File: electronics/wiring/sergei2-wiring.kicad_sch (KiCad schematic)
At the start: 27 parts, among them J1 6i25 port 1, J2 6i25 port 2, M1 UGRMEM, M2 UGRMEM, M3 MY1016, M4 Spindle, SW1 ESTOP, SW2 Mode switch, SW3 Run, SW4 Door closed, SW5 Pause, U1 Power_control_PCB

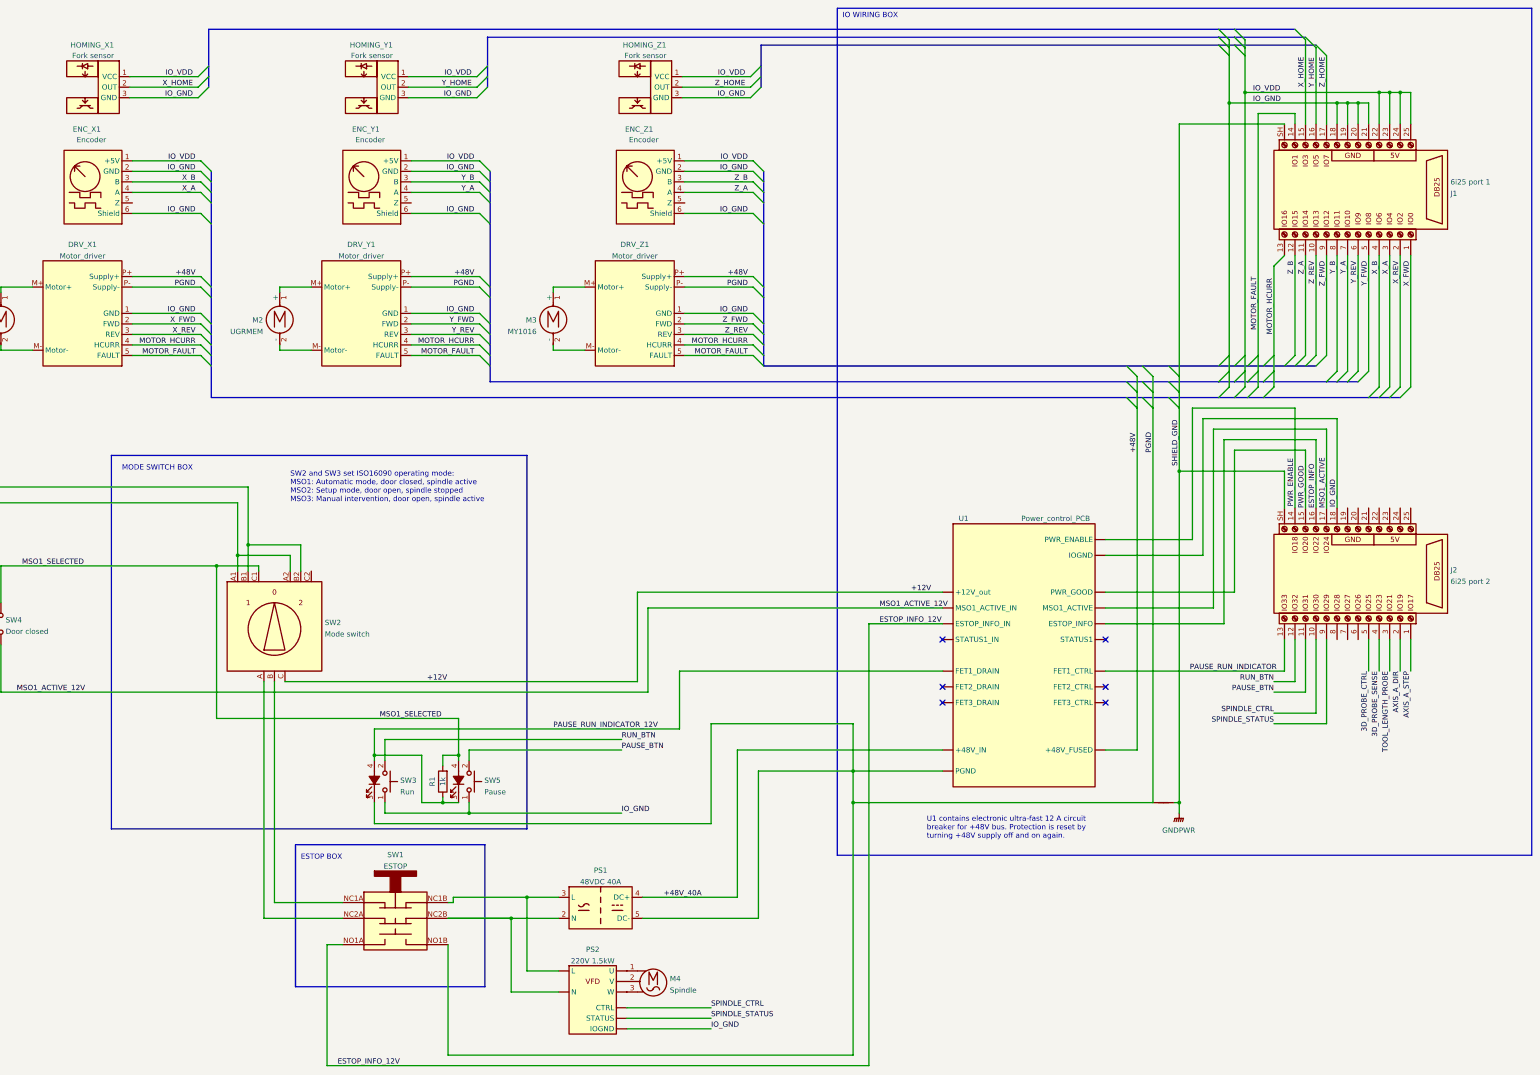
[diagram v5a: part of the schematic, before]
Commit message: Add PWM output for spindle control
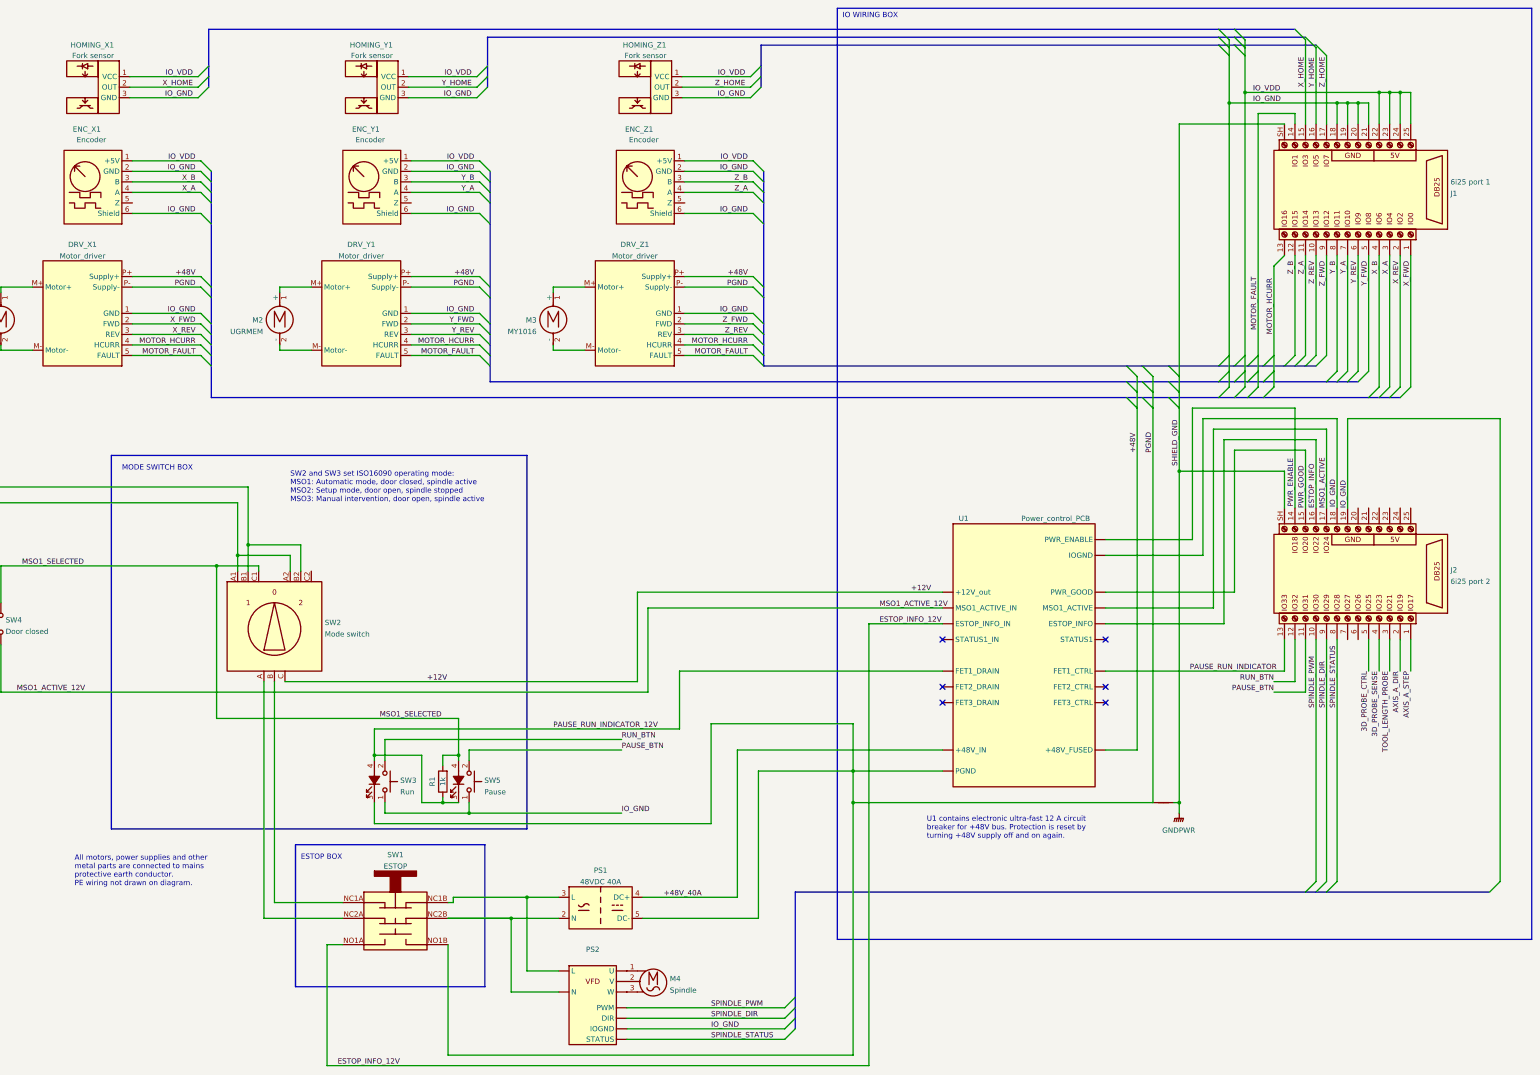
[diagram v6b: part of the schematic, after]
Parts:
- PS2: value 220V 1.5kW -> (none)
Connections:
- net IO_GND: now also J2.19
- net SPINDLE_STATUS: now also J2.8; no longer J2.9
- net SPINDLE_CTRL renamed SPINDLE_PWM
- new net SPINDLE_DIR: J2.9, PS2. (STATUS)
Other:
- note added: "All motors, power supplies and other metal parts are connected to mains protective earth conductor. PE wiring not drawn on diagram."

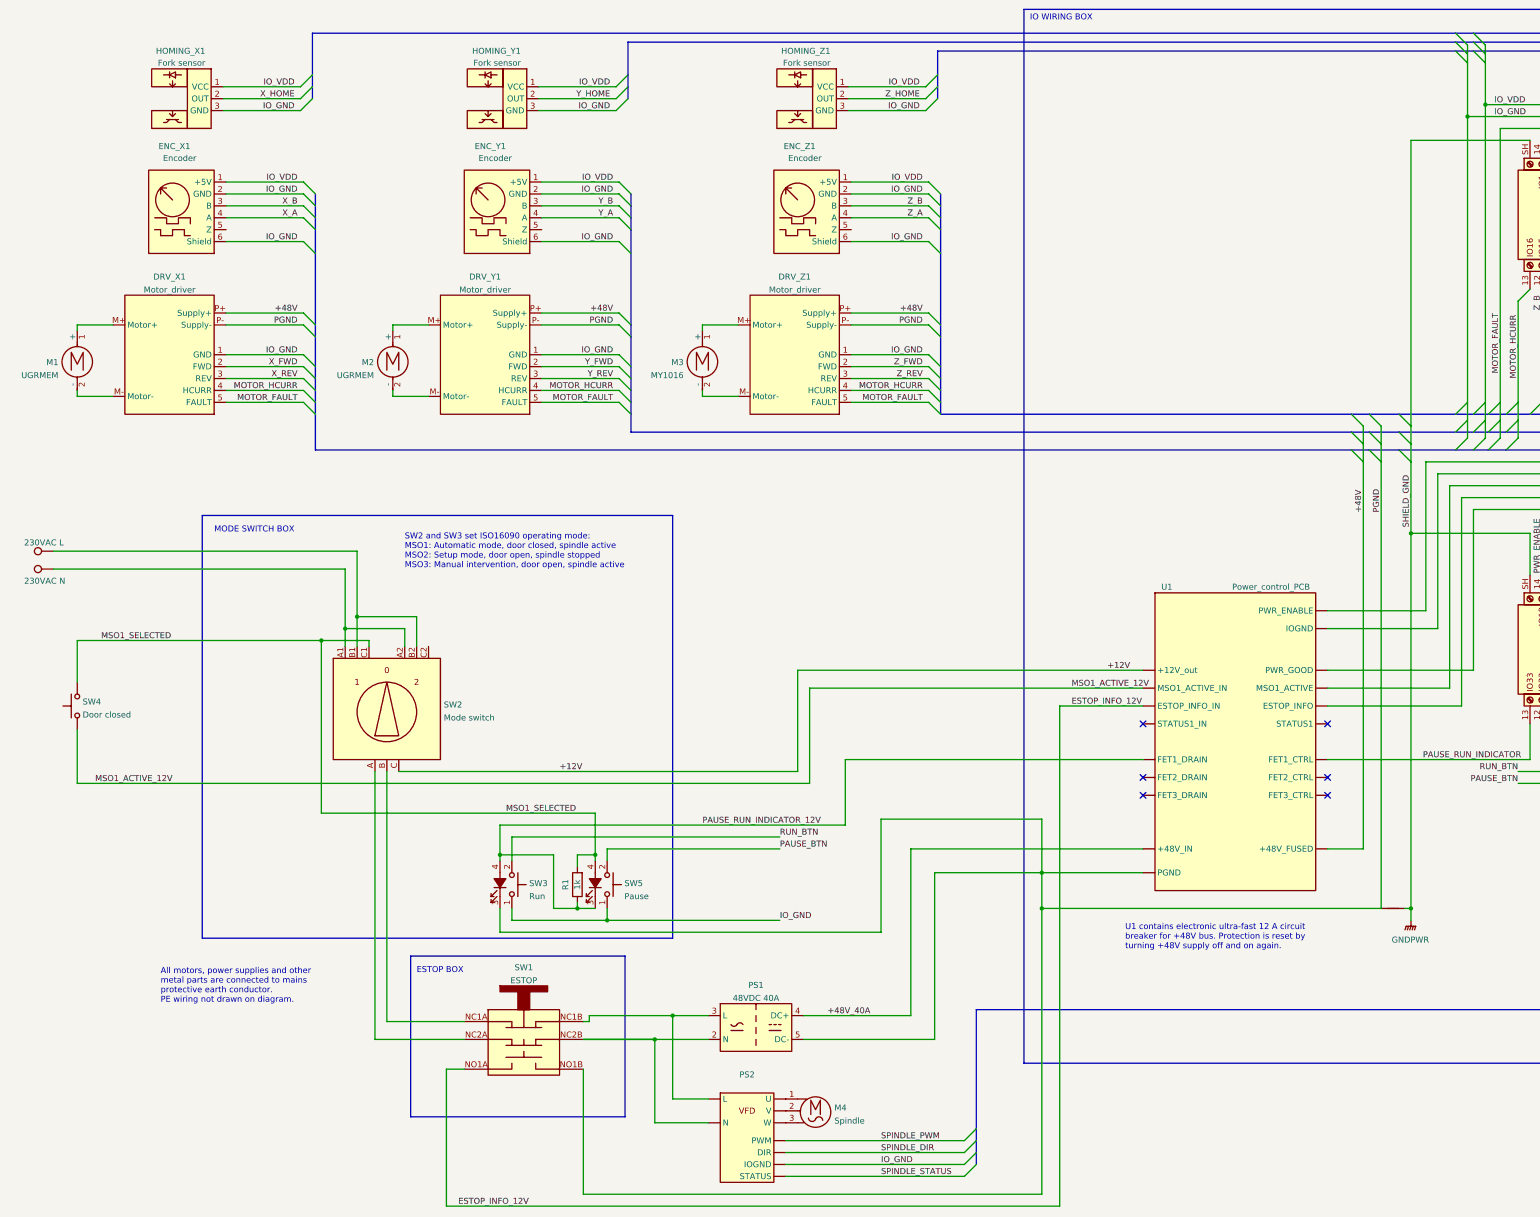
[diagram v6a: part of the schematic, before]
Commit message: Use FSESC 4.20 for driving Z axis, add brake shunt
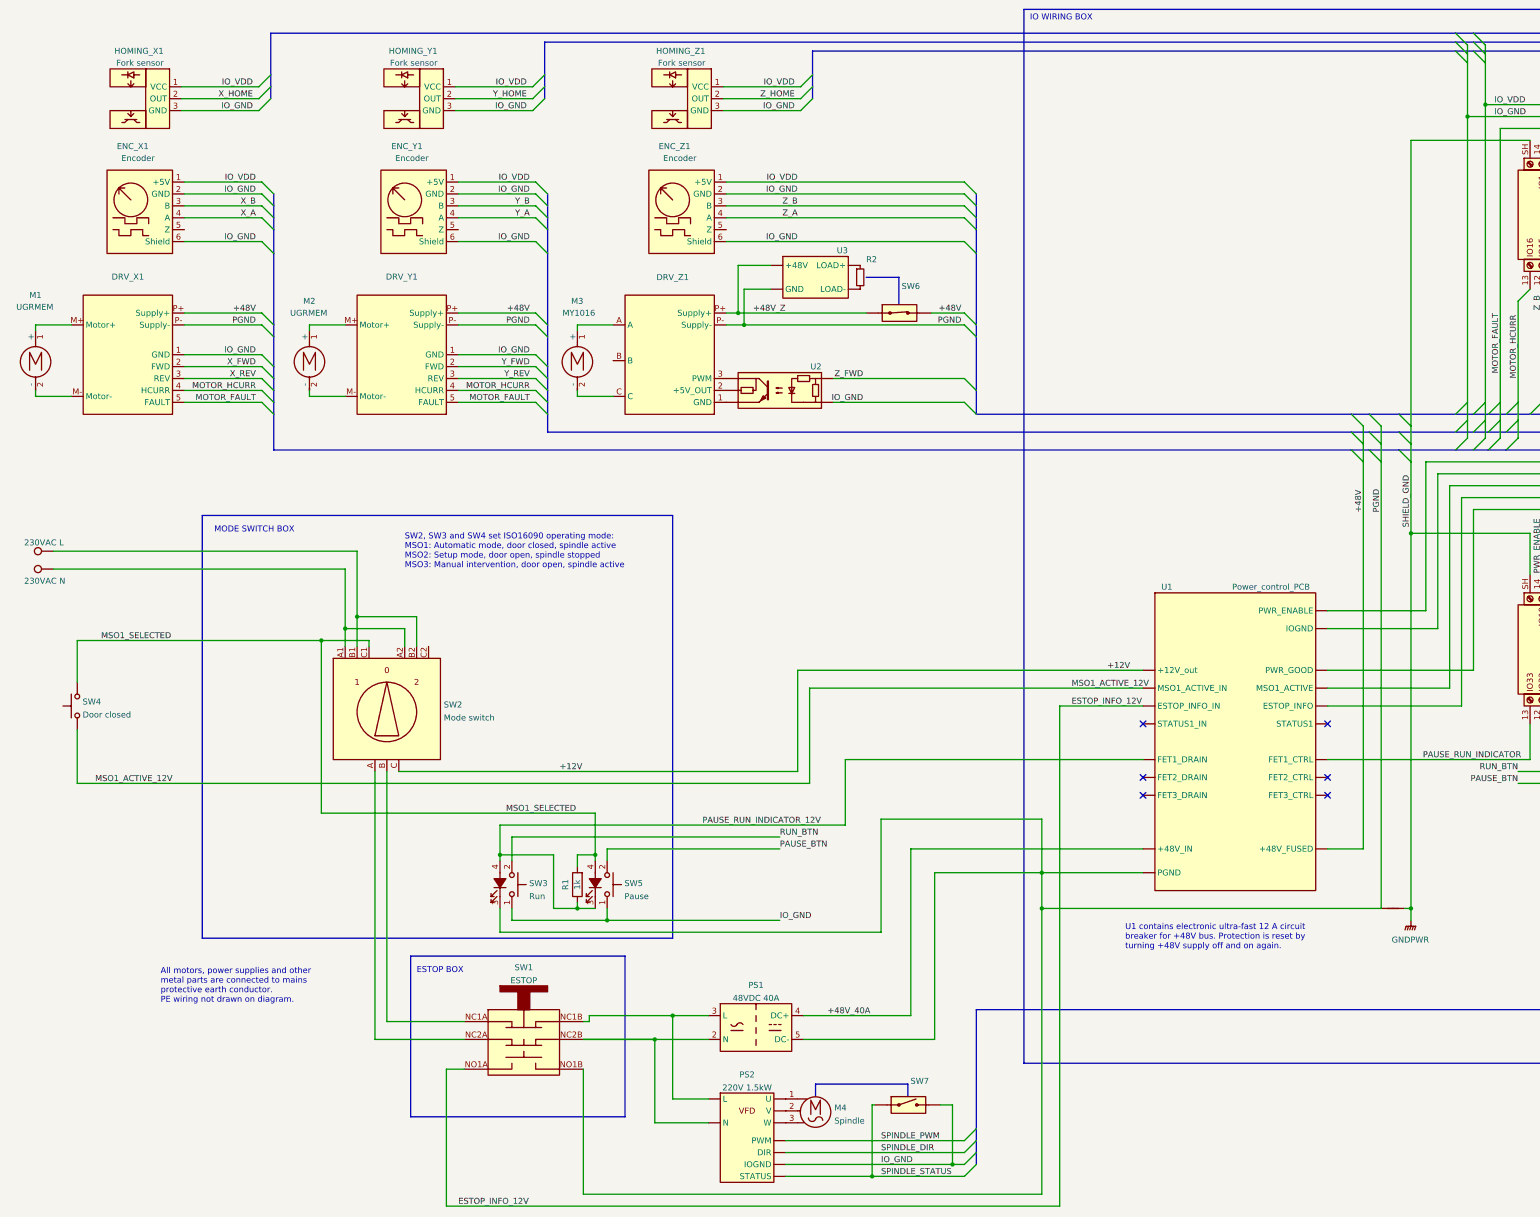
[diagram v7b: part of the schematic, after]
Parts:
- removed DRV_Z1: Motor_driver, symbol sergei2_wiring:Motor_driver
- added DRV_Z1: (no value), symbol sergei2_wiring:Motor_driver_FSESC
- added R2: (no value), symbol Device:R_Small
- added SW6: (no value), symbol sergei2_wiring:THERMAL_SW_NC
- added SW7: (no value), symbol sergei2_wiring:THERMAL_SW_NO
- added U2: (no value), symbol sergei2_wiring:OptoIsolator
- added U3: (no value), symbol sergei2_wiring:BrakeShunt
- DRV_X1, DRV_Y1: value Motor_driver -> (none)
- PS2: value (none) -> 220V 1.5kW
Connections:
- net +48V: now also SW6.
- net IO_GND: now also SW7., U2.2
- net PGND: now also DRV_Z1.P- (Supply-), U3. (LOAD-)
- net SPINDLE_STATUS: now also SW7.
- net Z_FWD: now also U2.1
- net at M3.1 (+): now also DRV_Z1.A
- net at M3.2 (-): now also DRV_Z1.C
- new net: DRV_Z1.1 (GND), U2.3
- new net: DRV_Z1.2 (+5V_OUT), U2.4
- new net: DRV_Z1.3 (PWM), U2.4
- new net: R2.1, U3. (LOAD-)
- new net: R2.2, U3. (LOAD-)
- new net +48V_Z: DRV_Z1.P+ (Supply+), SW6., U3. (LOAD-)
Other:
- note added: "SW2, SW3 and SW4 set ISO16090 operating mode: MSO1: Automatic mode, door closed, spindle active MSO2: Setup mode, door open, spindle stopped MSO3: Manual intervention, door open, spindle active"
- note removed: "SW2 and SW3 set ISO16090 operating mode: MSO1: Automatic mode, door closed, spindle active MSO2: Setup mode, door open, spindle stopped MSO3: Manual intervention, door open, spindle active"
- moved on the sheet: DRV_X1, DRV_Y1, ENC_X1, ENC_Y1, ENC_Z1, HOMING_X1, HOMING_Y1, HOMING_Z1, M1, M2, M3

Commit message: Misc configuration
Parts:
- removed SW6: (no value), symbol sergei2_wiring:THERMAL_SW_NC
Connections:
- net +48V: now also DRV_Z1.P+ (Supply+), U3. (LOAD-)
- removed net +48V_Z: DRV_Z1.P+ (Supply+), U3. (LOAD-)
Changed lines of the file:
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@@
   (junction (at 351.79 40.64) (diameter 0) (color 0 0 0 0)
   )
+  (junction (at 168.91 85.09) (diameter 0) (color 0 0 0 0)
+  )
   (junction (at 139.7 212.09) (diameter 0) (color 0 0 0 0)
   )
@@
   )
   (junction (at 213.36 264.16) (diameter 0) (color 0 0 0 0)
-  )
-  (junction (at 168.91 85.09) (diameter 0) (color 0 0 0 0)
   )
   (junction (at 361.95 38.1) (diameter 0) (color 0 0 0 0)
@@
     (stroke (width 0) (type default) (color 0 0 0 0))
   )
-  (wire (pts (xy 208.915 82.55) (xy 215.9 82.55))
-    (stroke (width 0) (type default) (color 0 0 0 0))
-  )
   (wire (pts (xy 124.46 96.52) (xy 107.95 96.52))
     (stroke (width 0) (type default) (color 0 0 0 0))
@@
     (stroke (width 0) (type default) (color 0 0 0 0))
   )
-  (wire (pts (xy 167.64 82.55) (xy 194.945 82.55))
+  (wire (pts (xy 167.64 82.55) (xy 215.9 82.55))
     (stroke (width 0) (type default) (color 0 0 0 0))
   )
@@
     (stroke (width 0.4) (type default) (color 0 0 0 1))
   )
-  (polyline (pts (xy 194.945 74.93) (xy 201.93 74.93))
-    (stroke (width 0) (type default) (color 0 0 0 0))
-  )
   (wire (pts (xy 361.95 109.22) (xy 361.95 77.47))
     (stroke (width 0) (type default) (color 0 0 0 0))
@@
     (stroke (width 0) (type default) (color 0 0 0 0))
   )
+  (wire (pts (xy 165.1 85.09) (xy 168.91 85.09))
+    (stroke (width 0) (type default) (color 0 0 0 0))
+  )
   (wire (pts (xy 364.49 45.72) (xy 364.49 38.1))
+    (stroke (width 0) (type default) (color 0 0 0 0))
+  )
+  (wire (pts (xy 168.91 85.09) (xy 215.9 85.09))
     (stroke (width 0) (type default) (color 0 0 0 0))
   )
@@
     (stroke (width 0) (type default) (color 0 0 0 0))
   )
-  (wire (pts (xy 165.1 85.09) (xy 168.91 85.09))
-    (stroke (width 0.4) (type default) (color 0 0 132 1))
-  )
   (bus (pts (xy 127 57.15) (xy 127 59.69))
     (stroke (width 0) (type default) (color 0 0 0 0))
@@
     (stroke (width 0) (type default) (color 0 0 0 0))
   )
-  (polyline (pts (xy 201.93 74.93) (xy 201.93 80.645))
-    (stroke (width 0) (type default) (color 0 0 0 0))
-  )
   (wire (pts (xy 344.17 101.6) (xy 344.17 77.47))
     (stroke (width 0) (type default) (color 0 0 0 0))
@@
     (stroke (width 0) (type default) (color 0 0 0 0))
   )
-  (wire (pts (xy 168.91 85.09) (xy 215.9 85.09))
-    (stroke (width 0.4) (type default) (color 0 0 132 1))
-  )
   (wire (pts (xy 196.215 251.46) (xy 196.85 251.46))
     (stroke (width 0) (type default) (color 0 0 0 0))
@@
     (effects (font (size 1.27 1.27)) (justify right bottom))
   )
-  (label "+48V_Z" (at 170.815 82.55 0)
-    (effects (font (size 1.27 1.27)) (justify left bottom))
-  )
   (label "3D_PROBE_SENSE" (at 359.41 177.8 270)
     (effects (font (size 1.27 1.27)) (justify right bottom))
@@
     (effects (font (size 1.27 1.27)) (justify right bottom))
   )
-  (label "PGND" (at 215.265 85.09 180)
+  (label "PGND" (at 214.63 85.09 180)
     (effects (font (size 1.27 1.27)) (justify right bottom))
   )
@@
     (pin "P-")
   )
-  (symbol (lib_id "sergei2_wiring:THERMAL_SW_NC") (at 201.93 82.55 0) (unit 1)
-    (in_bom yes) (on_board yes)
-    (property "Reference" "SW6" (id 0) (at 204.47 76.835 0))
-    (property "Value" "" (id 1) (at 207.01 78.74 0))
-    (property "Footprint" "" (id 2) (at 201.93 82.55 0)
-      (effects (font (size 1.27 1.27)) hide)
-    )
-    (property "Datasheet" "" (id 3) (at 201.93 82.55 0)
-      (effects (font (size 1.27 1.27)) hide)
-    )
-    (pin "")
-    (pin "")
-  )
   (symbol (lib_id "Motor:Motor_DC") (at 17.78 91.44 0) (mirror y) (unit 1)
     (in_bom yes) (on_board yes)
@@
     )
     (path "/efd0fcb6-86f3-407e-ae84-9f91a1cafffc"
-      (reference "R2") (unit 1) (value "15R") (footprint "")
+      (reference "R2") (unit 1) (value "10R") (footprint "")
     )
     (path "/bb00da48-0bcb-467b-972e-34490eb05b08"
@@
       (reference "SW5") (unit 1) (value "Pause") (footprint "")
     )
-    (path "/61af8392-13ec-4670-8fdf-002cf81d1317"
-      (reference "SW6") (unit 1) (value "90°C NC") (footprint "")
-    )
     (path "/4af3db05-c320-452b-a548-c79e418fc590"
